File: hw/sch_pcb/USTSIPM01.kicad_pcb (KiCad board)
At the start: 2 copper layers, 60 x 15 mm, 39 parts, among them J4 HEADER_2x01_PARALLEL, J5 HEADER_2x01_PARALLEL, J6 HEADER_2x01_PARALLEL, J8 HEADER_2x01_PARALLEL, J9 HEADER_2x01_PARALLEL, U1 MICROFC-60035-SMT-TR(1), U2 OPA836IDB, U3 MAX5026

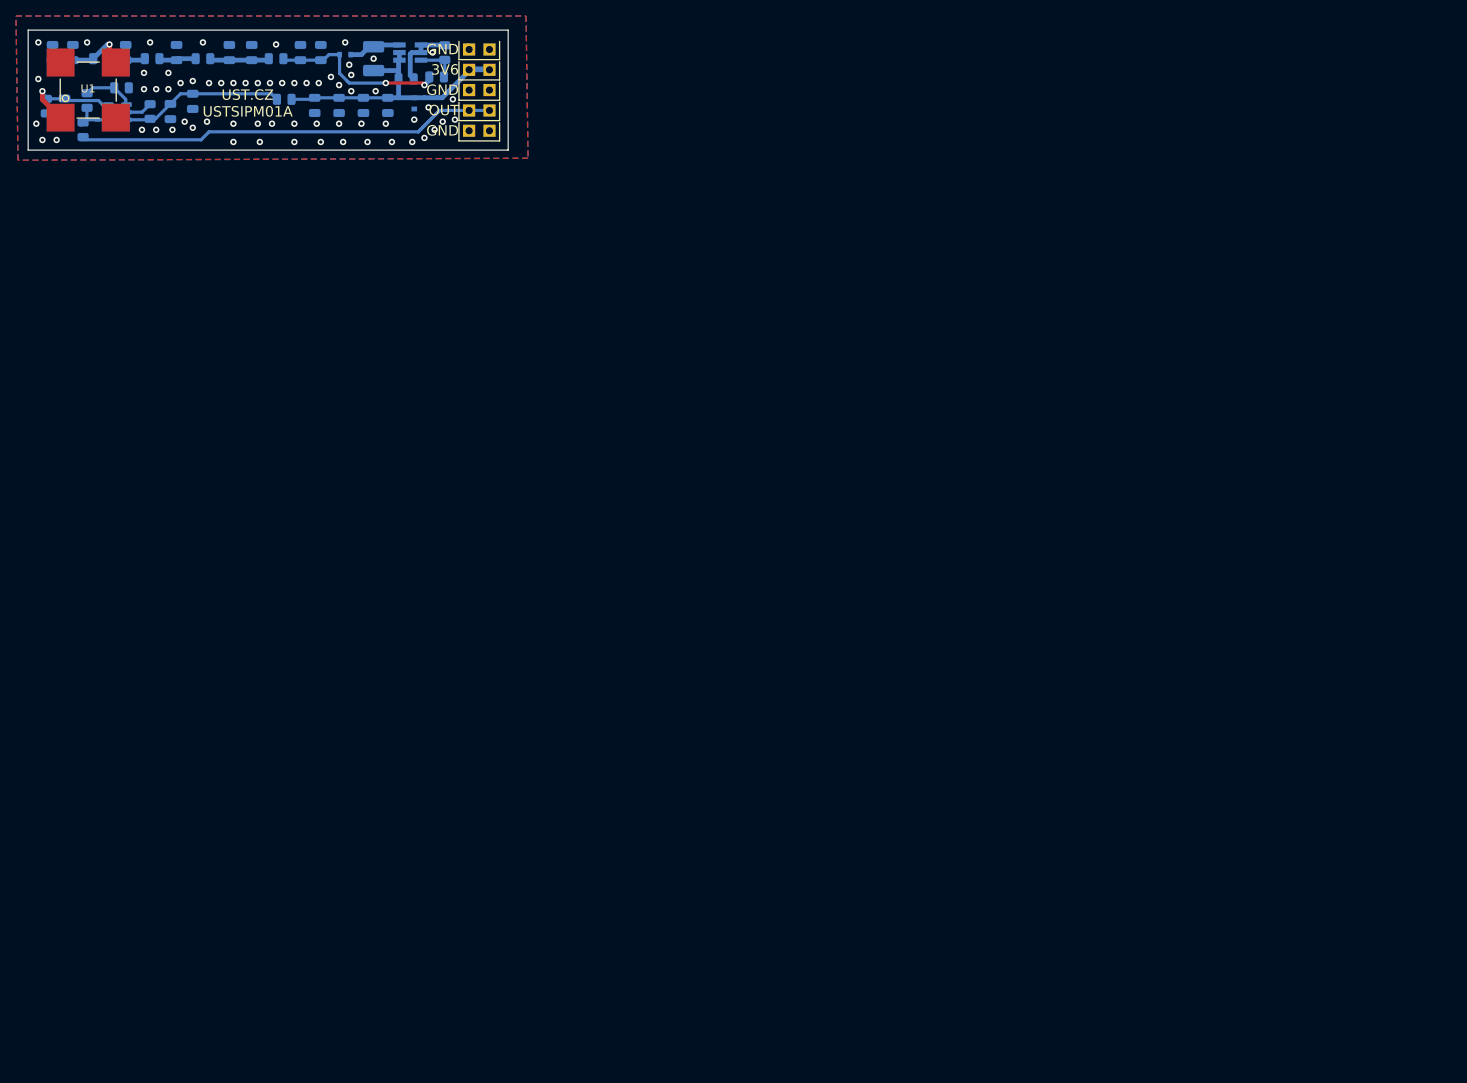
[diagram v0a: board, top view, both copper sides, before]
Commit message: Align schematics symbols to grid. Update PCB from schematic. Improve silkscreen. Move PCB to center of the page.
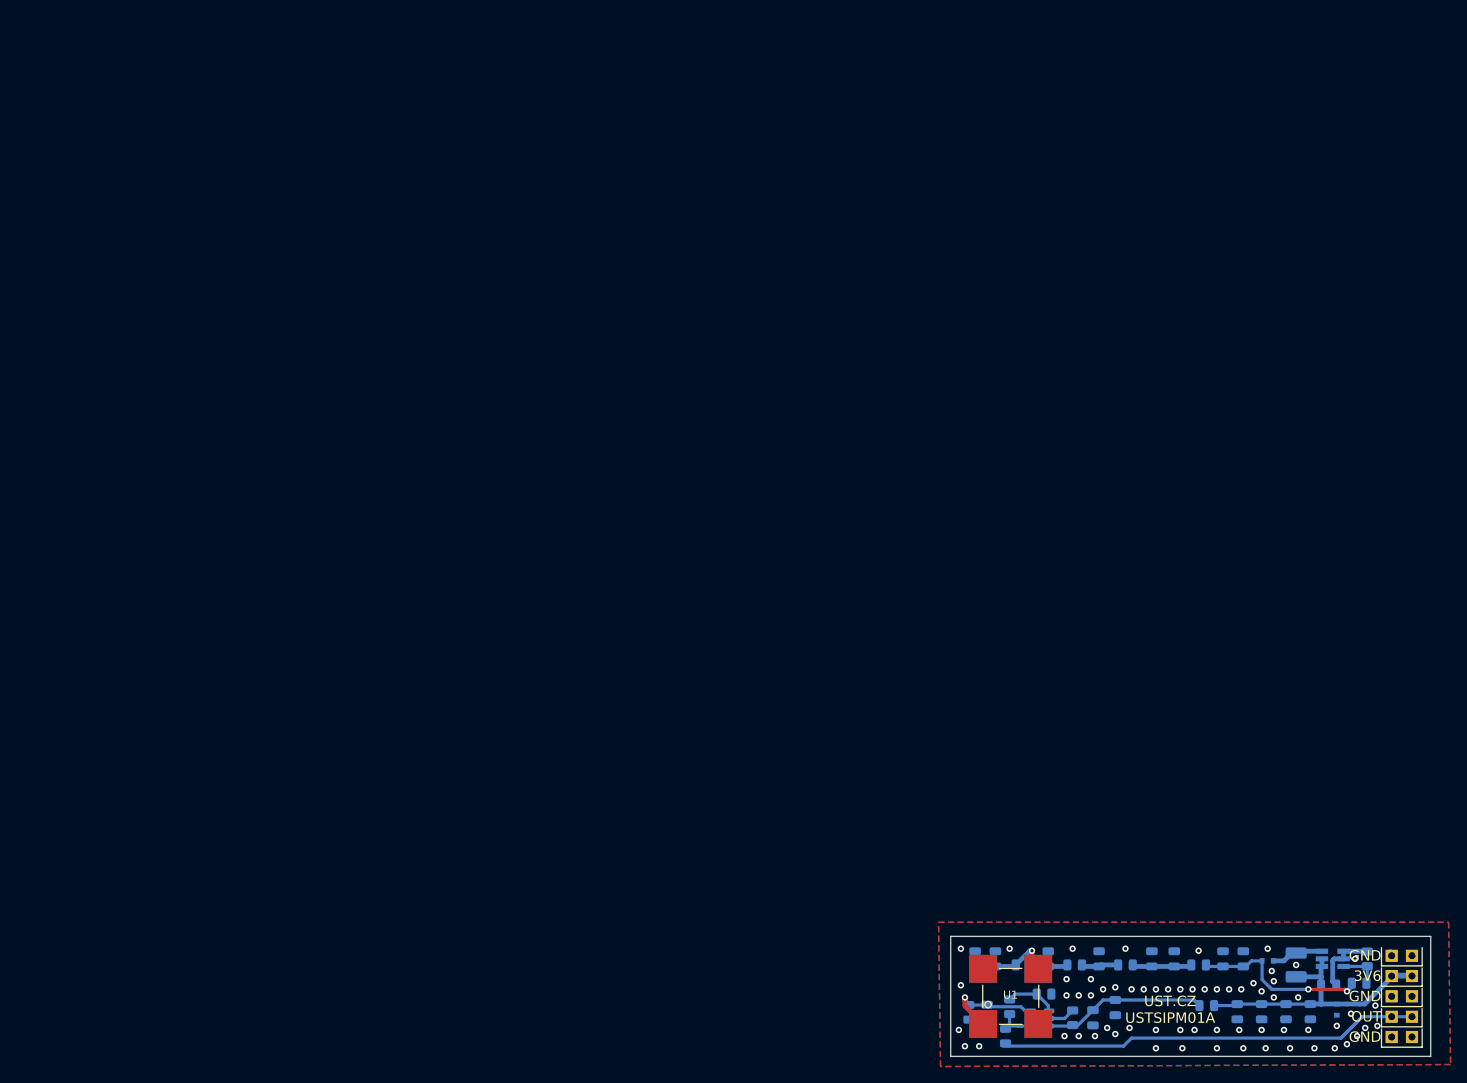
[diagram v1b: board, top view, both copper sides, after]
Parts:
- moved C2 161.7 mm to (162.6, 104.4)
- moved D2 161.7 mm to (154.9, 101.3)
- moved J4 161.7 mm to (171.7, 105.8)
- moved J9 161.7 mm to (171.7, 110.9)
- moved R10 161.7 mm to (122.7, 107.1)
- moved R11 161.7 mm to (130.6, 108.5)
- moved R12 161.7 mm to (122.2, 110.7)
- moved R6 161.7 mm to (166.4, 104.1)
- moved U1 161.7 mm to (122.8, 105.8)
- moved C1 161.7 mm to (133.9, 101.1)
- moved C10 161.7 mm to (151.9, 101.1)
- moved C11 161.7 mm to (149.4, 101.1)
- moved C12 161.7 mm to (143.3, 101.1)
- moved C13 161.7 mm to (140.5, 101.1)
- moved C14 161.7 mm to (157.2, 107.7)
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- renumbered R8 to C50
